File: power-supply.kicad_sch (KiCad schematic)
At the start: 107 parts

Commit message: Introduce component standardization
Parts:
- removed R75: (no value), symbol artix-dc-scm:R_200k_0402-artix-dc-scm
- added R75: R_200k_0402, antmicro-footprints:R_0402_1005Metric, symbol antmicroResistors0402:R_200k_0402
- C101, C103, C250, C83, C84, C85, C86, C87, C88, C89, C90: value (none) -> C_10u_0402; footprint (none) -> antmicro-footprints:C_0402_1005Metric; symbol artix-dc-scm:C_10u_0402 -> antmicroCapacitors0402:C_10u_0402; Author (none) -> Antmicro; License (none) -> Apache-2.0; MPN GRM155R60J106ME44D -> CC0402MRX5R5BB106; Manufacturer MURATA -> Yaego
- C14, C15, C16: value (none) -> C_10u_25V_0603; footprint (none) -> antmicro-footprints:C_0603_1608Metric; symbol artix-dc-scm:C_10u_25V_0603 -> antmicroCapacitors0603:C_10u_25V_0603; Author (none) -> Antmicro; License (none) -> Apache-2.0
- C2, C75, C76, C77, C78: value (none) -> C_10u_0603; footprint (none) -> antmicro-footprints:C_0603_1608Metric; symbol artix-dc-scm:C_10u_0402 -> antmicroCapacitors0603:C_10u_0603; Author (none) -> Antmicro; License (none) -> Apache-2.0; MPN GRM155R60J106ME44D -> GRM188R61A106KE69D; Manufacturer MURATA -> Murata
- C3, C79, C80, C81, C82: value (none) -> C_120p_0402; footprint (none) -> antmicro-footprints:C_0402_1005Metric; symbol artix-dc-scm:C_120p_0402 -> antmicroCapacitors0402:C_120p_0402; Author (none) -> Antmicro; License (none) -> Apache-2.0
- C64, C69: value (none) -> C_10n_0402; footprint (none) -> antmicro-footprints:C_0402_1005Metric; symbol artix-dc-scm:C_10n_0402 -> antmicroCapacitors0402:C_10n_0402; Author (none) -> Antmicro; Dielectric (none) -> X7R; License (none) -> Apache-2.0; MPN 04025G103ZAT2A -> GRM155R71H103KA88D; Manufacturer AVX -> Murata; Voltage (none) -> 50V
- C65, C66, C67: value (none) -> C_2u2_0603_25V; footprint (none) -> antmicro-footprints:C_0603_1608Metric; symbol artix-dc-scm:C_2u2_0603_25V -> antmicroCapacitorsmisc:C_2u2_0603_25V; Author (none) -> Antmicro; License (none) -> Apache-2.0; Manufacturer MURATA -> Murata
- C68: value (none) -> C_4n7_0402; footprint (none) -> antmicro-footprints:C_0402_1005Metric; symbol artix-dc-scm:C_4n7_0402 -> antmicroCapacitors0402:C_4n7_0402; Author (none) -> Antmicro; License (none) -> Apache-2.0
- C70: value (none) -> C_47p_0402; footprint (none) -> antmicro-footprints:C_0402_1005Metric; symbol artix-dc-scm:C_47p_0402 -> antmicroCapacitors0402:C_47p_0402; Author (none) -> Antmicro; Dielectric (none) -> C0G; License (none) -> Apache-2.0; MPN C0402C470J5GACTU -> GRM1555C1E470JA01D; Manufacturer KEMET -> Murata
- C71: value (none) -> C_100n_6V3_0402; footprint (none) -> antmicro-footprints:C_0402_1005Metric; symbol artix-dc-scm:C_100n_0402-artix-dc-scm -> antmicroCapacitorsmisc:C_100n_6V3_0402; Author (none) -> Antmicro; License (none) -> Apache-2.0
- C72, C73, C74: value (none) -> C_47u_0603; footprint (none) -> antmicro-footprints:C_0603_1608Metric; symbol artix-dc-scm:C_47u_0603 -> antmicroCapacitors0603:C_47u_0603; Author (none) -> Antmicro; License (none) -> Apache-2.0; Manufacturer MURATA -> Murata
- D14, D4, D5, D6, D7, D8: value (none) -> LED_G_0603_LG_L29K-G2J1-24-Z; footprint (none) -> antmicro-footprints:LED_0603_1608Metric_G; symbol artix-dc-scm:LG_L29K-G2J1-24-Z -> antmicroLEDIndicationDiscrete:LED_G_0603_LG_L29K-G2J1-24-Z; Author (none) -> Antmicro; License (none) -> Apache-2.0; Manufacturer OSRAM Opto Semiconductors Inc. -> Osram
- D3: value (none) -> PDS760; footprint (none) -> antmicro-footprints:PowerDI5; symbol artix-dc-scm:PDS760-13 -> antmicroDiodesRectifiersSingle:PDS760; Author (none) -> Antmicro; License (none) -> Apache-2.0; Manufacturer Diodes Inc. -> Diodes Incorporated
- F1: value (none) -> 0466003.NR; footprint (none) -> antmicro-footprints:F_1206_3216Metric; symbol artix-dc-scm:0466003.NR -> antmicroFuses:F_3A_1206; Author (none) -> Antmicro; License (none) -> Apache-2.0
- IC1: value (none) -> TPS54561QDPR; footprint (none) -> antmicro-footprints:WSON-10_4x4; symbol artix-dc-scm:TPS54561 -> antmicroPMICVoltageRegulatorsLinear:TPS54561QDPRRQ1; Author (none) -> Antmicro; License (none) -> Apache-2.0; MPN TPS54561-Q1 -> TPS54561QDPRRQ1; Manufacturer Texas Instrumets -> Texas Instruments
- J10, J5: value (none) -> Molex_Pico-Lock_1x02_504050-0291; footprint (none) -> antmicro-footprints:Molex_Pico-Lock_504050-0291_1x02_1MP_P1.5mm; symbol artix-dc-scm:5040500291 -> antmicroRectangularConnectorsHeadersMalePins:Molex_Pico-Lock_1x02_504050-0291; Author (none) -> Antmicro; License (none) -> Apache-2.0; MANUFACTURER Molex -> (none); Manufacturer (none) -> Molex
- L1: value (none) -> 7447798720; footprint (none) -> antmicro-footprints:L_4141_WE_PDF; symbol artix-dc-scm:WE_7447798720 -> antmicroFixedInductors:7447798720; Author (none) -> Antmicro; License (none) -> Apache-2.0; Manufacturer Wurth Elektronik -> Würth Elektronik; Size (none) -> 10.2x10.2; Val (none) -> 7u2/7.9A
- L2, L3, L4, L5, L6: value (none) -> IHLP1212AEERR47M11; footprint (none) -> antmicro-footprints:L_Vishay_IHLP-1212; symbol artix-dc-scm:IHLP1212AEERR47M11 -> antmicroFixedInductors:IHLP1212AEERR47M11; Author (none) -> Antmicro; License (none) -> Apache-2.0; Size (none) -> 3.0x3.0; Val (none) -> 470n/6.7A
- Q1, Q2, Q3, Q4, Q5, Q6: value (none) -> BSS138PW; footprint (none) -> antmicro-footprints:SC70-3; symbol artix-dc-scm:BSS138APW -> antmicroTransistorsFETsMOSFETsSingle:BSS138PW; Author (none) -> Antmicro; License (none) -> Apache-2.0; Manufacturer ON Semiconductor -> Nexperia
- R138, R14, R15, R16, R185: value (none) -> R_0R_0402; footprint (none) -> antmicro-footprints:R_0402_1005Metric; symbol artix-dc-scm:R_0R_0402 -> antmicroResistors0402:R_0R_0402; Author (none) -> Antmicro; Current (none) -> 1A; License (none) -> Apache-2.0; Manufacturer PANASONIC -> Panasonic
- R139, R140, R141, R142, R188: value (none) -> R_0R_0603; footprint (none) -> antmicro-footprints:R_0603_1608Metric; symbol artix-dc-scm:R_0R_0603 -> antmicroResistors0603:R_0R_0603; Author (none) -> Antmicro; Current (none) -> 1A; License (none) -> Apache-2.0; Manufacturer BOURNS -> Bourns
- R186, R187, R63, R64, R65, R68, R74, R76, R78, R80: value (none) -> R_100k_0402; footprint (none) -> antmicro-footprints:R_0402_1005Metric; symbol artix-dc-scm:R_100k_0402 -> antmicroResistors0402:R_100k_0402; Author (none) -> Antmicro; License (none) -> Apache-2.0; MPN CRCW0402100KFKEDHP -> CR0402-FX-1003GLF; Manufacturer VISHAY -> Bourns; Tolerance (none) -> 1%
- R189, R61, R91, R92, R93: value (none) -> R_10k_0402; footprint (none) -> antmicro-footprints:R_0402_1005Metric; symbol artix-dc-scm:R_10k_0402 -> antmicroResistors0402:R_10k_0402; Author (none) -> Antmicro; License (none) -> Apache-2.0; MPN CRCW040210K0FKEDHP -> CR0402-FX-1002GLF; Manufacturer VISHAY -> Bourns; Tolerance (none) -> 1%
- R190, R94, R95, R96, R97, R98: value (none) -> R_1k_0402; footprint (none) -> antmicro-footprints:R_0402_1005Metric; symbol artix-dc-scm:R_1k_0402 -> antmicroResistors0402:R_1k_0402; Author (none) -> Antmicro; License (none) -> Apache-2.0; Manufacturer BOURNS -> Bourns; Tolerance (none) -> 1%
- R66: value (none) -> R_16k9_0402; footprint (none) -> antmicro-footprints:R_0402_1005Metric; symbol artix-dc-scm:R_16k9_0402 -> antmicroResistors0402:R_16k9_0402; Author (none) -> Antmicro; License (none) -> Apache-2.0; MPN ERA2AEB1692X -> CR0402-FX-1692GLF; Manufacturer PANASONIC -> Bourns; Tolerance (none) -> 1%
- R67: value (none) -> R_243k_0402; footprint (none) -> antmicro-footprints:R_0402_1005Metric; symbol artix-dc-scm:R_243k_0402 -> antmicroResistors0402:R_243k_0402; Author (none) -> Antmicro; License (none) -> Apache-2.0; MPN MCMR04X2433FTL -> CR0402-FX-2433GLF; Manufacturer MULTICOMP -> Bourns; Tolerance (none) -> 1%
- R69: value (none) -> R_0R_1206; footprint (none) -> antmicro-footprints:R_1206_3216Metric; symbol artix-dc-scm:R_0R_1206 -> antmicroResistorsmisc:R_0R_1206; Author (none) -> Antmicro; Current (none) -> 2A; License (none) -> Apache-2.0; Manufacturer MULTICOMP -> Multicomp
- R70: value (none) -> R_49R9_0402; footprint (none) -> antmicro-footprints:R_0402_1005Metric; symbol artix-dc-scm:R_49R9_0402 -> antmicroResistors0402:R_49R9_0402; Author (none) -> Antmicro; License (none) -> Apache-2.0; MPN CRCW040249R9FKED -> CR0402-FX-49R9GLF; Manufacturer VISHAY -> Bourns; Tolerance (none) -> 1%
- R71: value (none) -> R_53k6_0402; footprint (none) -> antmicro-footprints:R_0402_1005Metric; symbol artix-dc-scm:R_53k6_0402 -> antmicroResistors0402:R_53k6_0402; Author (none) -> Antmicro; License (none) -> Apache-2.0; MPN CPF0402B53K6E1_ -> CR0402-FX-5362GLF; Manufacturer TE_CONNECTIVITY -> Bourns; Tolerance (none) -> 1%
- R72: value (none) -> R_10k2_0402; footprint (none) -> antmicro-footprints:R_0402_1005Metric; symbol artix-dc-scm:R_10k2_0402 -> antmicroResistors0402:R_10k2_0402; Author (none) -> Antmicro; License (none) -> Apache-2.0; MPN MCWR04X1022FTL -> CR0402-FX-1022GLF; Manufacturer MULTICOMP -> Bourns; Tolerance (none) -> 1%
- R73: value (none) -> R_453k_0402; footprint (none) -> antmicro-footprints:R_0402_1005Metric; symbol artix-dc-scm:R_453k_0402 -> antmicroResistors0402:R_453k_0402; Author (none) -> Antmicro; License (none) -> Apache-2.0; MPN CRCW0402453KFKED -> CR0402-FX-4533GLF; Manufacturer VISHAY -> Bourns; Tolerance (none) -> 1%
- R77: value (none) -> R_66k5_0402; footprint (none) -> antmicro-footprints:R_0402_1005Metric; symbol artix-dc-scm:R_66k5_0402 -> antmicroResistors0402:R_66k5_0402; Author (none) -> Antmicro; License (none) -> Apache-2.0; MPN ERJ2RKF6652X -> CR0402-FX-6652GLF; Manufacturer PANASONIC -> Bourns; Tolerance (none) -> 1%
- R79: value (none) -> R_124k_0402; footprint (none) -> antmicro-footprints:R_0402_1005Metric; symbol artix-dc-scm:R_124k_0402 -> antmicroResistors0402:R_124k_0402; Author (none) -> Antmicro; License (none) -> Apache-2.0; MPN WR04X1243FTL -> CR0402-FX-1243GLF; Manufacturer WALSIN -> Bourns; Tolerance (none) -> 1%
- TP1, TP4: value (none) -> TP_SMD1MM; footprint (none) -> antmicro-footprints:Testpoint_smd_1mm; symbol artix-dc-scm:TP_SMD1MM -> antmicroTestPoints:TP_1mm_SMD; Author (none) -> Antmicro; DNP (none) -> DNP; License (none) -> Apache-2.0
- U10, U11, U12, U13, U16: value (none) -> TPS62823DLCT; footprint (none) -> antmicro-footprints:QFN-8_2x1mm; symbol artix-dc-scm:TPS62823DLCT -> antmicroDCDCConverters:TPS62823DLCT; Author (none) -> Antmicro; License (none) -> Apache-2.0
- U9: value (none) -> LM3881MME_NOPB; footprint (none) -> antmicro-footprints:VSSOP-8_3x3mm_P0.65mm; symbol artix-dc-scm:LM3881MME_NOPB -> antmicroPMICPowerSequencers:LM3881MME_NOPB; Author (none) -> Antmicro; License (none) -> Apache-2.0
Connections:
- net 5V0_PG: now also C250.2; no longer C250.1
- net GND: now also C101.1, C103.1, C14.1, C15.1, C16.1, C2.1, C250.1, C64.1, C65.1, C66.1, C67.1, C68.1, C69.1, C70.1, C72.1, C73.1, C74.1, C75.1, C76.1, C77.1, C78.1, C83.1, C84.1, C85.1, C86.1, C87.1, C88.1, C89.1, C90.1, J10.SH, J5.SH; no longer C101.2, C103.2, C14.2, C15.2, C16.2, C2.2, C250.2, C64.2, C65.2, C66.2, C67.2, C68.2, C69.2, C70.2, C72.2, C73.2, C74.2, C75.2, C76.2, C77.2, C78.2, C83.2, C84.2, C85.2, C86.2, C87.2, C88.2, C89.2, C90.2, J10.S1 (SHIELD), J10.S2 (SHIELD__1), J5.S1 (SHIELD), J5.S2 (SHIELD__1)
- net VCC12V: now also C14.2, C15.2, C16.2, C65.2, C66.2, C67.2; no longer C14.1, C15.1, C16.1, C65.1, C66.1, C67.1
- net VCC5V0: now also C2.2, C75.2, C76.2, C77.2, C78.2; no longer C2.1, C75.1, C76.1, C77.1, C78.1
- net at L1.2, R69.2, R70.1: now also C72.2, C73.2, C74.2; no longer C72.1, C73.1, C74.1
- net at R186.2, R187.1, U16.2 (FB): now also C3.1; no longer C3.2
- net at L6.2, R186.1, R188.2: now also C101.2, C103.2, C3.2; no longer C101.1, C103.1, C3.1
- net at L2.2, R139.2, R73.1: now also C79.2, C83.2, C87.2; no longer C79.1, C83.1, C87.1
- net at L5.2, R142.2, R79.1: now also C82.2, C86.2, C90.2; no longer C82.1, C86.1, C90.1
- net at L4.2, R141.2, R77.1: now also C81.2, C85.2, C89.2; no longer C81.1, C85.1, C89.1
- net at IC1.1 (BOOT): now also C71.1; no longer C71.2
- net at IC1.4 (SS/TR): now also C69.2; no longer C69.1
- net at IC1.7 (COMP), R66.1: now also C70.2; no longer C70.1
- net at D3.C, IC1.9 (SW), L1.1: now also C71.2; no longer C71.1
- net at R66.2: now also C68.2; no longer C68.1
- net at U9.5 (TADJ): now also C64.2; no longer C64.1
- net at R77.2, R78.1, U12.2 (FB): now also C81.1; no longer C81.2
- net at R73.2, R74.1, U10.2 (FB): now also C79.1; no longer C79.2
- net at R76.1, U11.2 (FB): now also C80.1, R75.1; no longer C80.2
- net at R79.2, R80.1, U13.2 (FB): now also C82.1; no longer C82.2
- new net: C80.2, C84.2, C88.2, L3.2, R140.2, R75.2
- no-connect marks 1 -> 0
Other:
- note added: "DC-SCM 12V supply"
- note added: "To DC-SCM connector"
- moved on the sheet: C101, C103, C14, C15, C16, C2, C250, C3, C64, C65, C66, C67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

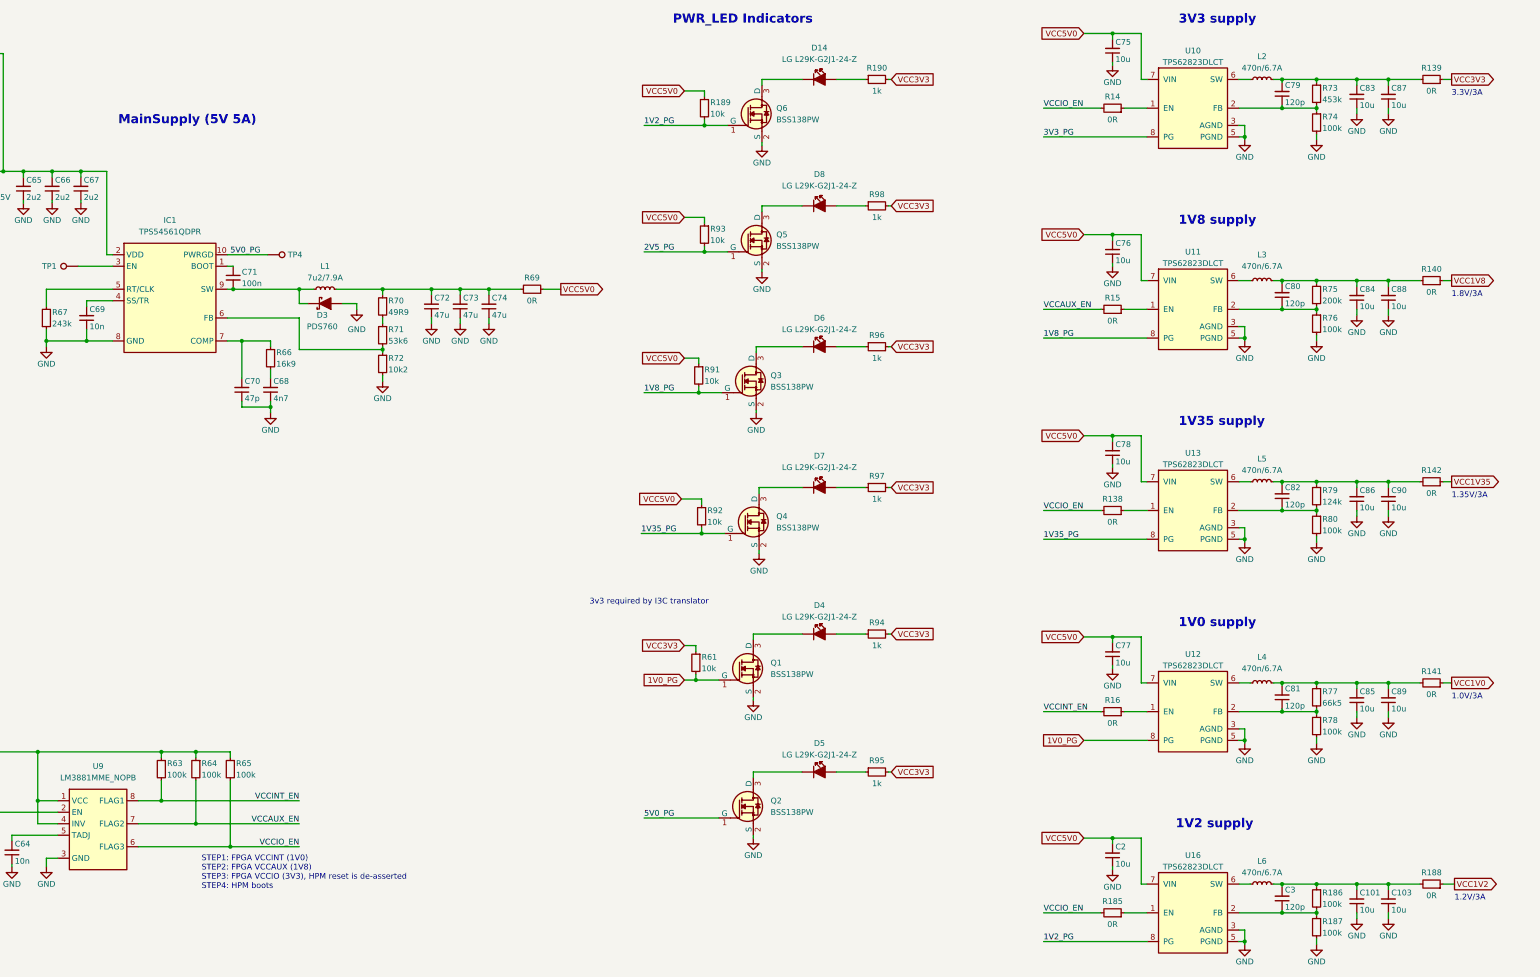
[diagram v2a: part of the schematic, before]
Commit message: Fix schematic ERC errors. ERC clean
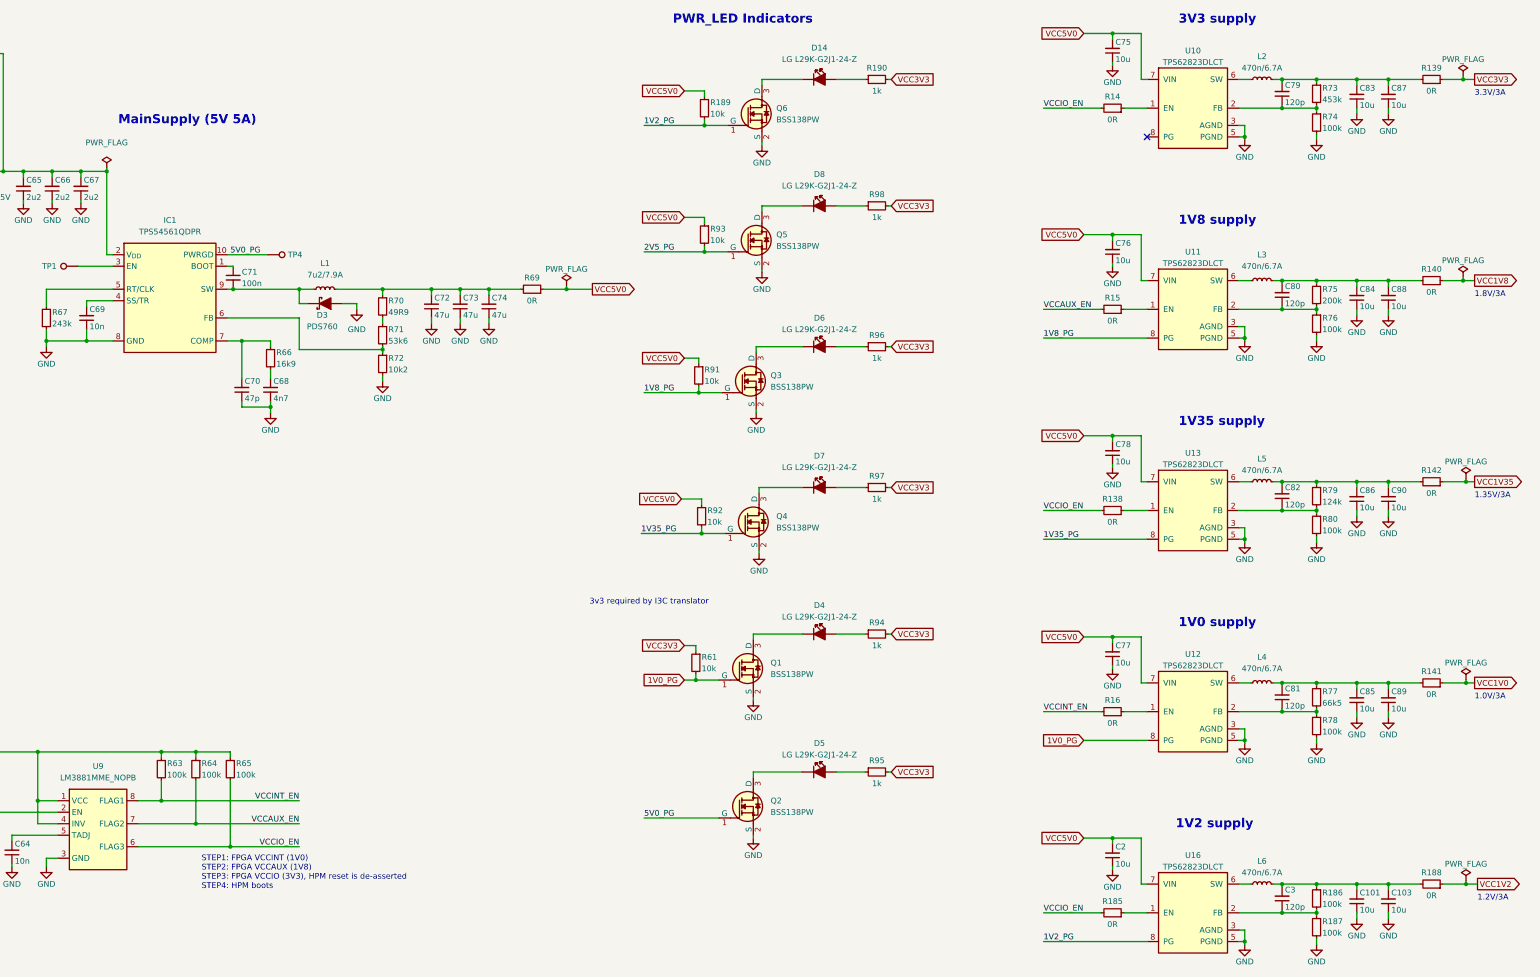
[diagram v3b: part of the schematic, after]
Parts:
- L1: footprint antmicro-footprints:L_4141_WE_PDF -> antmicro-footprints:L_WE-PDF; symbol antmicroFixedInductors:7447798720 -> antmicroFixedInductors:L_7u2_7.9A_WE-PDF
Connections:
- net 3V3_PG: no longer names the net of U10.8 (PG)
- no-connect marks 0 -> 1
